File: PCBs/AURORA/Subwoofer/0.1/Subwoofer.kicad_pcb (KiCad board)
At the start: 2 copper layers, 65 x 55 mm, 47 parts, among them J1 Conn_01x02_Pin, J2 Conn_01x02_Pin, J3 Conn_01x02_Pin, J4 Conn_01x03_Pin, J5 Conn_01x03_Pin, J6 Conn_01x03_Male, J7 Conn_01x02_Pin, J8 Conn_01x03_Male, J9 Conn_01x02_Pin, T1 Transformer_Audio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

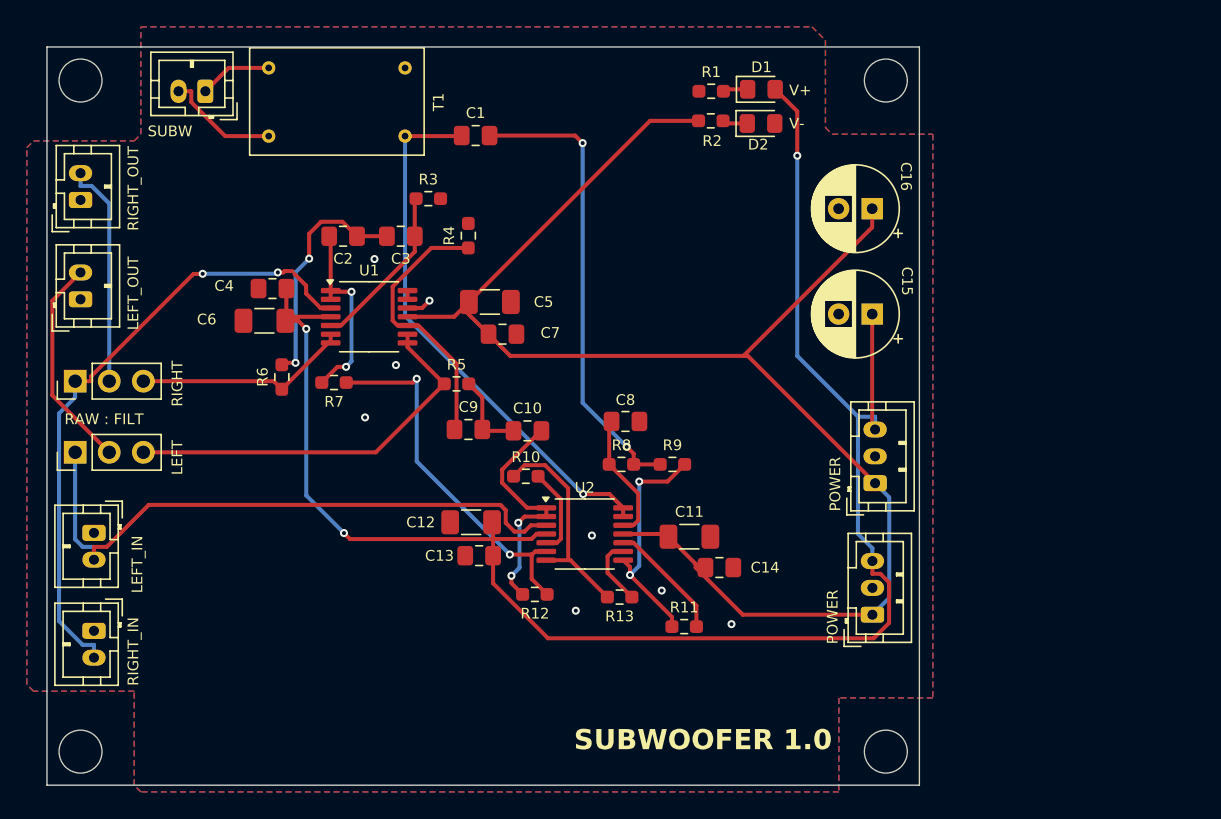
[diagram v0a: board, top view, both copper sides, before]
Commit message: Fixing audio issues, leave TRUNC off and at 24 bits
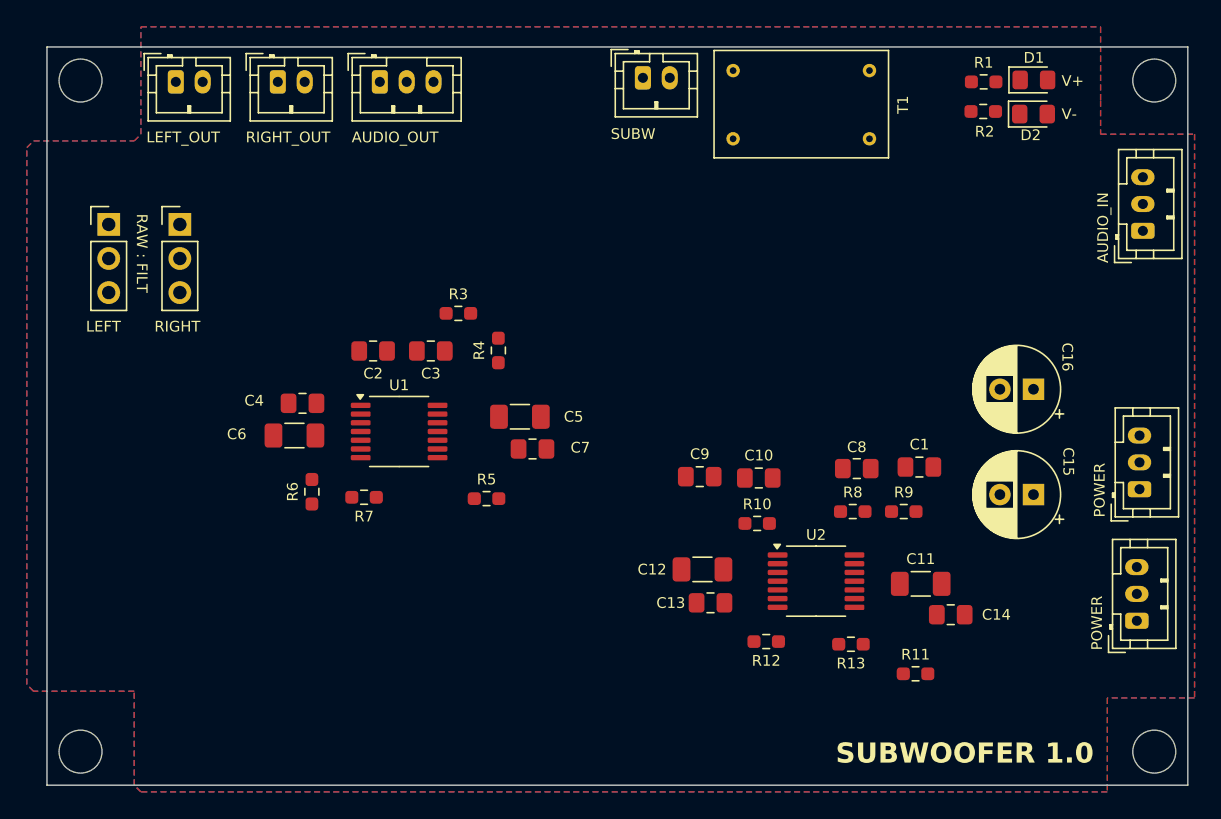
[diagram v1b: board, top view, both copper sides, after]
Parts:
- removed J9: Conn_01x02_Pin, Connector_JST:JST_PH_B2B-PH-K_1x02_P2.00mm_Vertical
- added J10: Conn_01x03_Pin, Connector_JST:JST_PH_B3B-PH-K_1x03_P2.00mm_Vertical, F.Cu at (188.1, 74.9)
- J7: value Conn_01x02_Pin -> Conn_01x03_Pin; footprint Connector_JST:JST_PH_B2B-PH-K_1x02_P2.00mm_Vertical -> Connector_JST:JST_PH_B3B-PH-K_1x03_P2.00mm_Vertical
- moved C1 41.3 mm to (171.4, 92.5)
- moved J7 39.8 mm to (131.2, 63.8), turned to 0 degrees
- moved T1 34.6 mm to (162.6, 65.5)
- moved J1 32.6 mm to (150.8, 63.5), turned to 0 degrees
- moved R2 20.3 mm to (176.2, 66.0)
- moved D1 20.3 mm to (180.0, 63.6)
- moved D2 20.3 mm to (179.9, 66.2)
- moved R1 20.3 mm to (176.2, 63.8)
- moved H2 20.0 mm to (188.9, 63.7)
- moved H4 20.0 mm to (188.9, 113.7)
- moved J8 19.7 mm to (187.6, 103.9)
- moved J6 19.7 mm to (187.8, 94.1)
- moved C15 18.0 mm to (179.9, 94.5)
- moved C16 18.0 mm to (179.9, 86.7)
- moved J3 17.7 mm to (116.0, 63.8), turned to 0 degrees
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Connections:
- J7 pad 1: AGND -> LEFT_OUT
- J7 pad 2: LEFT_IN -> AGND
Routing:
- net V+: track 130.1 -> 0.00 mm, vias 3 -> 0
- net V-: track 110.8 -> 0.00 mm
- net LEFT_IN: track 46.6 -> 0.00 mm
- net RIGHT_IN: track 46.6 -> 0.00 mm, vias 2 -> 0
- net SUBW: track 40.5 -> 0.00 mm, vias 1 -> 0
- net Net-(C1-Pad2): track 34.7 -> 0.00 mm, vias 2 -> 0
- net LEFT_FILT: track 29.4 -> 0.00 mm
- net Net-(U2B--): track 27.6 -> 0.00 mm, vias 2 -> 0
- net Net-(U1C-+): track 20.4 -> 0.00 mm
- net Net-(U2A--): track 18.1 -> 0.00 mm, vias 2 -> 0
- net Net-(C2-Pad1): track 17.7 -> 0.00 mm, vias 2 -> 0
- net Net-(R11-Pad1): track 17.6 -> 0.00 mm, vias 2 -> 0
- net RIGHT_OUT: track 16.9 -> 0.00 mm
- net RIGHT_FILT: track 16.3 -> 0.00 mm
- net Net-(R10-Pad1): track 16.2 -> 0.00 mm
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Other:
- board size 65 x 55 mm -> 85 x 55 mm
- board text added: "AUDIO_IN"
- board text added: "AUDIO_OUT"
- board text removed: "LEFT_IN"
- board text removed: "RIGHT_IN"
